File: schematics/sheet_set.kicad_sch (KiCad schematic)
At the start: 0 parts

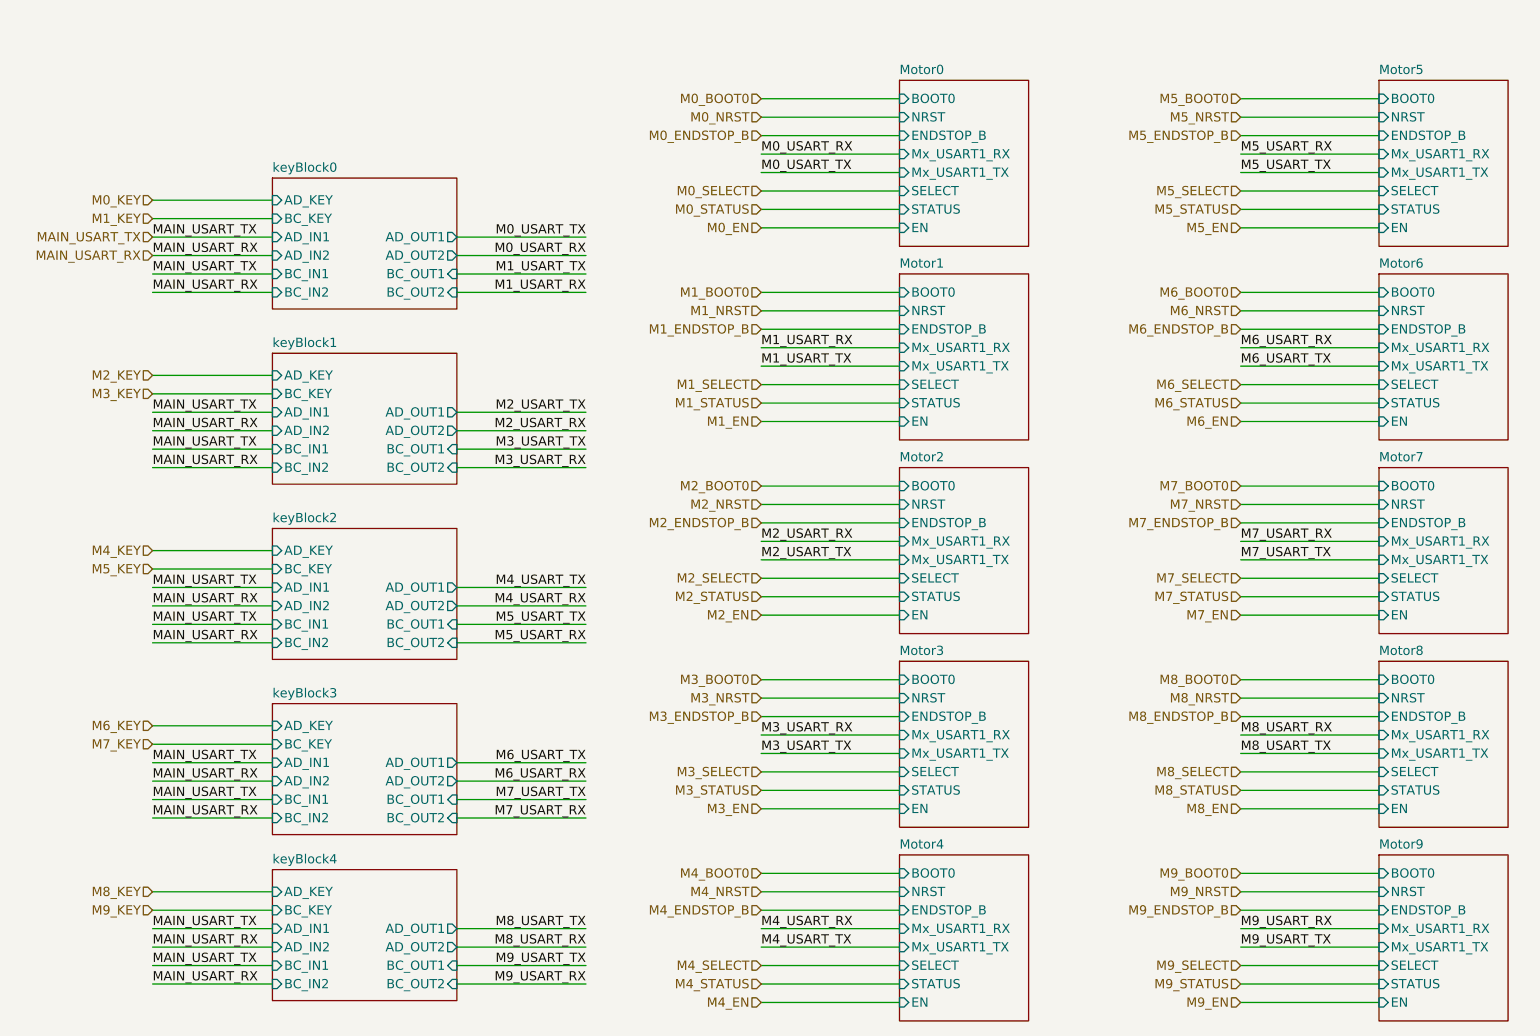
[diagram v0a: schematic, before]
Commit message: Обновил схемотехнику у платы. Убрал лишнее компоненты и лишнии линии
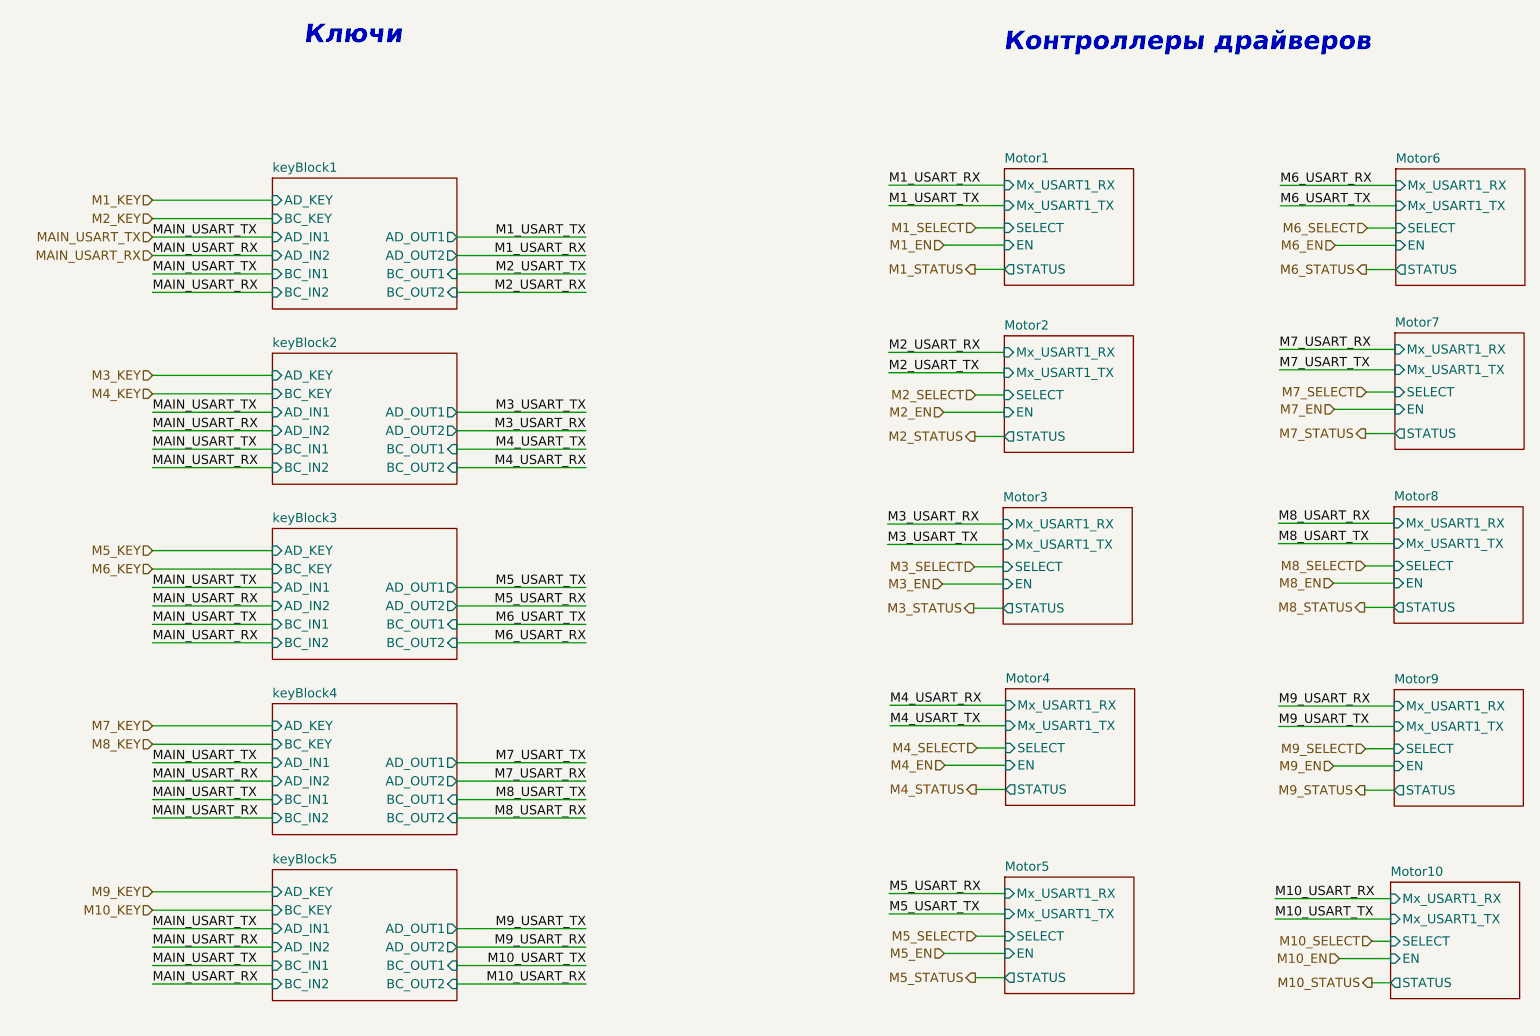
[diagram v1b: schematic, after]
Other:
- removed sheet Motor0
- removed sheet keyBlock0
- added sheet Motor10 (Motor.kicad_sch)
- added sheet keyBlock5 (keyBlock.kicad_sch)
- sheet Motor1 ports: added none; removed BOOT0, ENDSTOP_B, NRST
- sheet Motor2 ports: added none; removed BOOT0, ENDSTOP_B, NRST
- sheet Motor3 ports: added none; removed BOOT0, ENDSTOP_B, NRST
- sheet Motor4 ports: added none; removed BOOT0, ENDSTOP_B, NRST
- sheet Motor5 ports: added none; removed BOOT0, ENDSTOP_B, NRST
- sheet Motor6 ports: added none; removed BOOT0, ENDSTOP_B, NRST
- sheet Motor7 ports: added none; removed BOOT0, ENDSTOP_B, NRST
- sheet Motor8 ports: added none; removed BOOT0, ENDSTOP_B, NRST
- sheet Motor9 ports: added none; removed BOOT0, ENDSTOP_B, NRST
- note added: "Ключи"
- note added: "Контроллеры драйверов"
- company: (none) -> МГТУ им. Н.Э.Баумана
